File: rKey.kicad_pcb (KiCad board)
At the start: 2 copper layers, 52.8 x 66.8 mm, 42 parts, among them IC1 BDX34C, IC2 BDX34C, J1 Conn_01x03, Q1 BC337, Q2 BC337, Q3 BC337, Q4 BC337, Q5 BC327, Q8 BC337, U1 TL084BCN, U2 LM7810_TO220

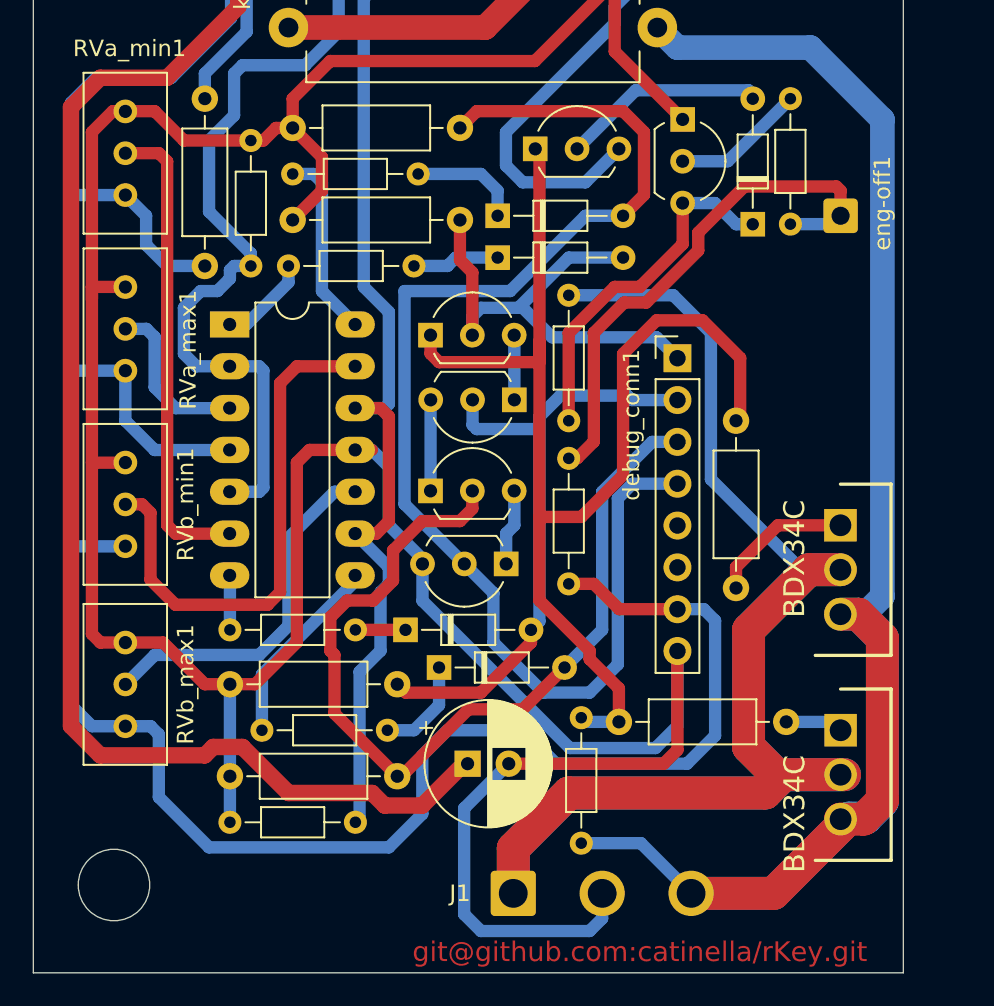
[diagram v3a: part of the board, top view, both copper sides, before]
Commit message: Fix: wrong resistors power size
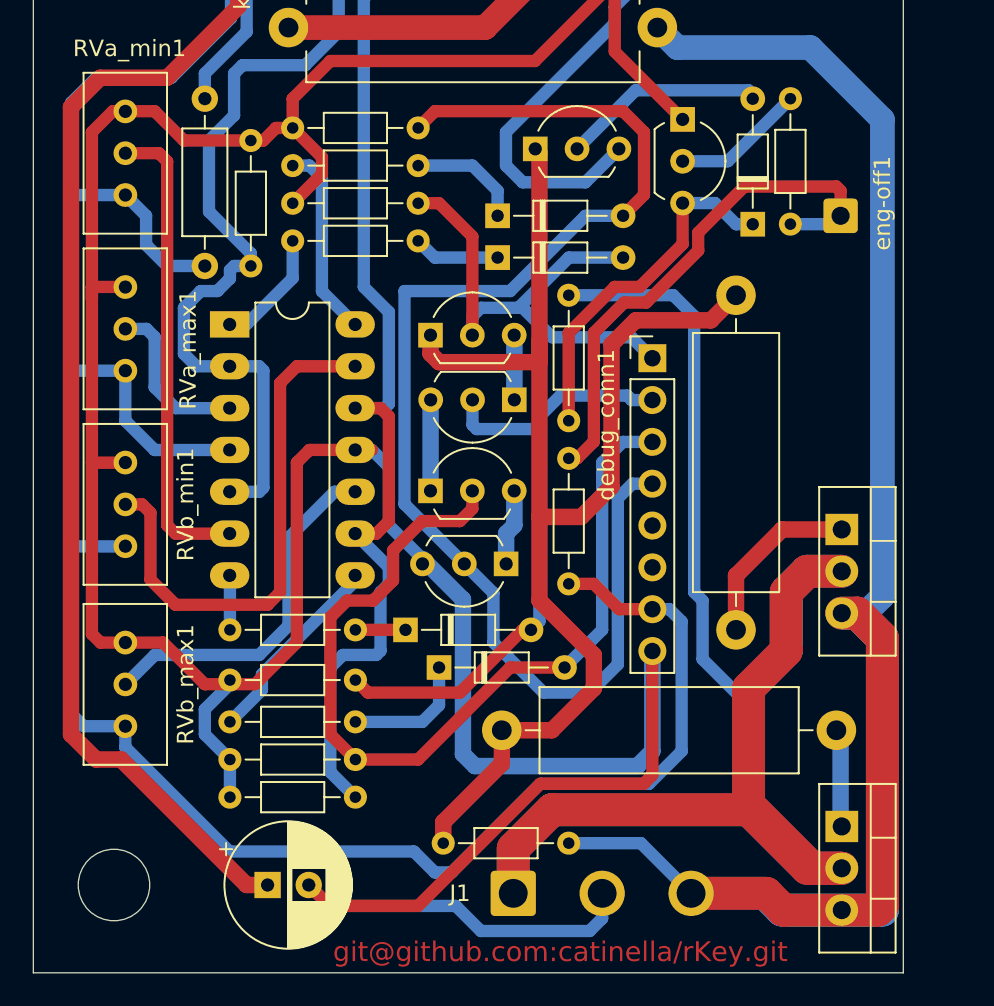
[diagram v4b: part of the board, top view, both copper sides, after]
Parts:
- removed IC1, IC2: BDX34C, BDX34C:TO270P460X1020X2008-3P
- added Q6: D45VH10, Package_TO_SOT_THT:TO-220-3_Vertical, F.Cu at (165.7, 96.5)
- added Q7: D45VH10, Package_TO_SOT_THT:TO-220-3_Vertical, F.Cu at (165.7, 114.6)
- R10, R18: value 1.6K -> 100; footprint Resistor_THT:R_Axial_DIN0207_L6.3mm_D2.5mm_P10.16mm_Horizontal -> Resistor_THT:R_Axial_DIN0516_L15.5mm_D5.0mm_P20.32mm_Horizontal
- R12, R15, R16, R17: footprint Resistor_THT:R_Axial_DIN0207_L6.3mm_D2.5mm_P10.16mm_Horizontal -> Resistor_THT:R_Axial_DIN0204_L3.6mm_D1.6mm_P7.62mm_Horizontal
- moved C1 14.2 mm to (130.8, 118.1)
- moved R18 7.62 mm to (159.3, 82.3)
- moved R10 7.13 mm to (145.0, 108.7)
- moved R4 2.01 mm to (128.5, 108.2)
- moved R2 1.55 mm to (132.3, 79.0)
- moved R8 1.52 mm to (136.1, 112.8)
- moved debug_conn1 1.52 mm to (154.2, 86.1)
- moved R15 1.02 mm to (132.3, 76.7)
- moved R16 1.02 mm to (128.5, 110.5)
- moved R11 0.76 mm to (149.1, 115.6), turned to 180 degrees
- moved R5 0.51 mm to (132.3, 74.4)
- moved R17 0.25 mm to (128.5, 105.7)
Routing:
- net GND: track 234.6 -> 253.1 mm
- net Net-(J1-Pad1): track 119.3 -> 132.7 mm
- net Net-(C1-Pad1): track 116.5 -> 105.2 mm
- net Net-(J1-Pad3): track 110.1 -> 119.7 mm
- net Net-(R1-Pad1): track 167.9 -> 160.7 mm
- net Net-(Q1-Pad1): track 74.7 -> 81.0 mm
- net Net-(R10-Pad2): track 3.51 -> 5.87 mm
- net Net-(R18-Pad2): track 8.66 -> 10.9 mm
- net Net-(R4-Pad2): track 6.05 -> 7.79 mm
- net Net-(R2-Pad1): track 5.63 -> 7.25 mm
- net Net-(Q1-Pad2): track 29.7 -> 31.0 mm
- net Net-(Q4-Pad2): track 80.1 -> 81.1 mm
- net Net-(R8-Pad1): track 62.7 -> 63.6 mm
- net Net-(Q2-Pad2): track 38.2 -> 38.9 mm

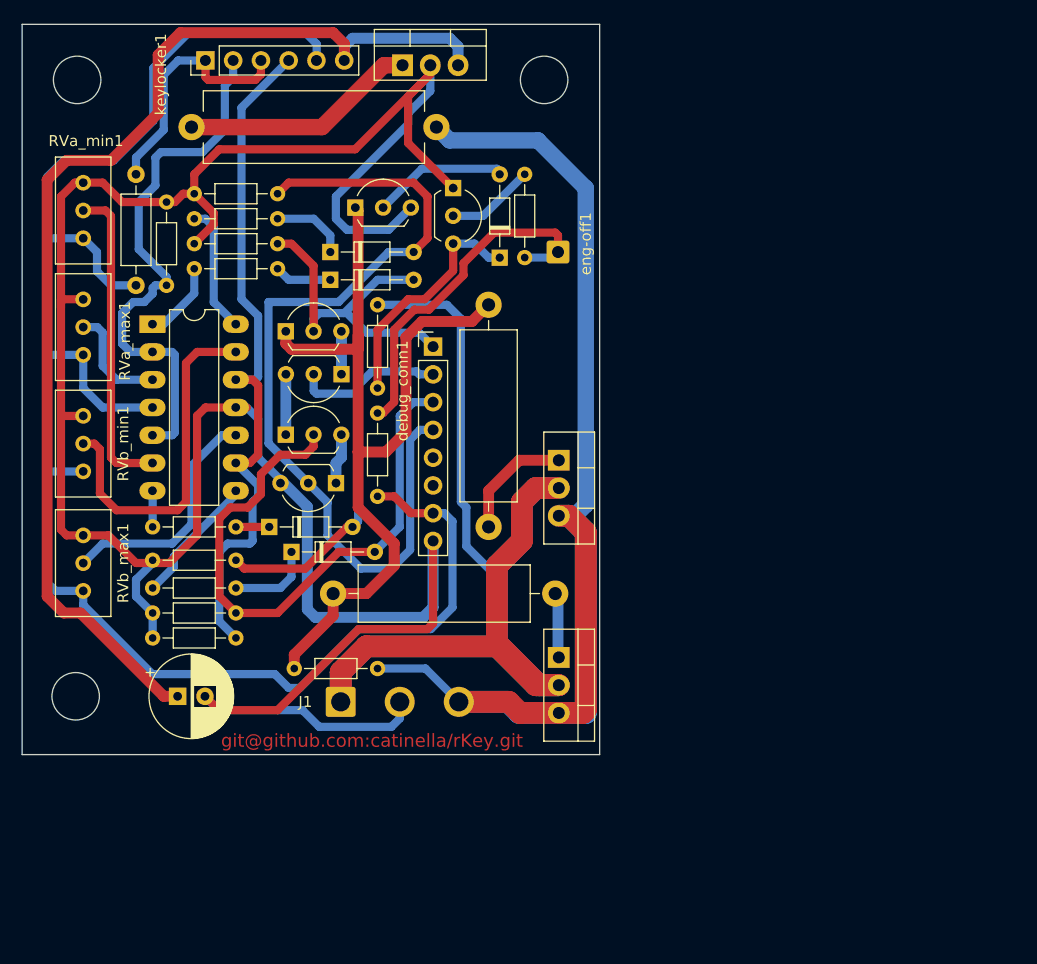
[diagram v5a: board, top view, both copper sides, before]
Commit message: Feat: Circuit for engine locking when vehicle is off
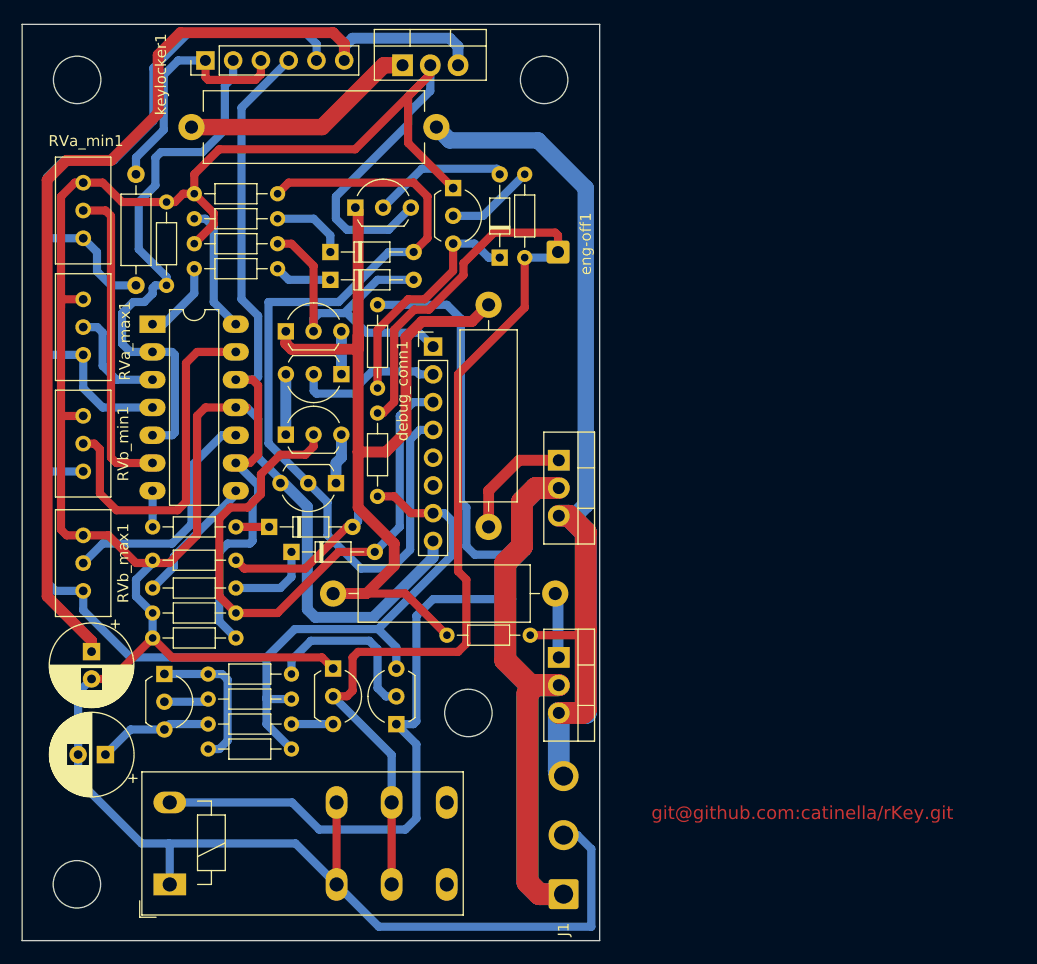
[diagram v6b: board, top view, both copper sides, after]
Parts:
- added C2: 2uF, Capacitor_THT:CP_Radial_D7.5mm_P2.50mm, F.Cu at (124.2, 123.4)
- added K1: RT42xxxx, Relay_THT:Relay_DPDT_Schrack-RT2-FormC_RM5mm, F.Cu at (130.1, 135.3)
- added Q10: BC337, Package_TO_SOT_THT:TO-92L_Inline_Wide, F.Cu at (129.6, 116.1)
- added Q11: BC327, Package_TO_SOT_THT:TO-92L_Inline_Wide, F.Cu at (145.0, 115.6)
- added Q9: BC327, Package_TO_SOT_THT:TO-92L_Inline_Wide, F.Cu at (150.8, 120.7)
- added R19: 60K, Resistor_THT:R_Axial_DIN0204_L3.6mm_D1.6mm_P7.62mm_Horizontal, F.Cu at (133.6, 118.4)
- added R20: 20K, Resistor_THT:R_Axial_DIN0204_L3.6mm_D1.6mm_P7.62mm_Horizontal, F.Cu at (133.6, 116.1)
- added R21: 2K, Resistor_THT:R_Axial_DIN0204_L3.6mm_D1.6mm_P7.62mm_Horizontal, F.Cu at (133.6, 120.7)
- added R22: 200K, Resistor_THT:R_Axial_DIN0204_L3.6mm_D1.6mm_P7.62mm_Horizontal, F.Cu at (141.2, 122.9)
- moved J1 26.9 mm to (166.1, 136.2), turned to 90 degrees
- moved R11 14.3 mm to (163.1, 112.5)
- moved C1 8.87 mm to (122.9, 114.0), turned to -90 degrees
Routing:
- net Net-(R13-Pad2): track 32.7 -> 106.3 mm
- net Net-(J1-Pad1): track 132.7 -> 186.5 mm
- net GND: track 253.1 -> 305.9 mm
- net Net-(J1-Pad3): track 119.7 -> 103.1 mm
- net Net-(Q9-Pad2): track 0.00 -> 15.8 mm
- net Net-(Q10-Pad1): track 0.00 -> 13.7 mm
- net Net-(R1-Pad1): track 160.7 -> 171.6 mm
- net Net-(C2-Pad1): track 0.00 -> 10.6 mm
- net Net-(C1-Pad1): track 105.2 -> 96.2 mm
- net Net-(Q10-Pad2): track 0.00 -> 4.11 mm
- net Net-(Q11-Pad3): track 0.00 -> 3.81 mm
- net Net-(Q1-Pad1): track 81.0 -> 84.7 mm
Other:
- board size 52.8 x 66.8 mm -> 52.8 x 83.8 mm

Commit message: fixes
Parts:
- added R23: 10K, Resistor_THT:R_Axial_DIN0204_L3.6mm_D1.6mm_P5.08mm_Horizontal, F.Cu at (148.3, 122.9)
- moved K1 0.25 mm to (130.1, 135.1)
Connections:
- K1 pad 11: Net-(R13-Pad2) -> Net-(K1-Pad11)
- K1 pad 21: Net-(R13-Pad2) -> Net-(K1-Pad11)
- Q11 pad 2: Net-(R13-Pad2) -> Net-(Q11-Pad2)
- R13 pad 2: Net-(R13-Pad2) -> Net-(K1-Pad11)
- R14 pad 2: Net-(R13-Pad2) -> Net-(K1-Pad11)
- eng-off1 pad 1: Net-(R13-Pad2) -> Net-(K1-Pad11)
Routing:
- net Net-(R13-Pad2): track 106.3 -> 0.00 mm
- net Net-(K1-Pad11): track 0.00 -> 100.9 mm
- net Net-(Q11-Pad2): track 0.00 -> 6.64 mm
- net Net-(Q9-Pad3): track 171.6 -> 173.7 mm

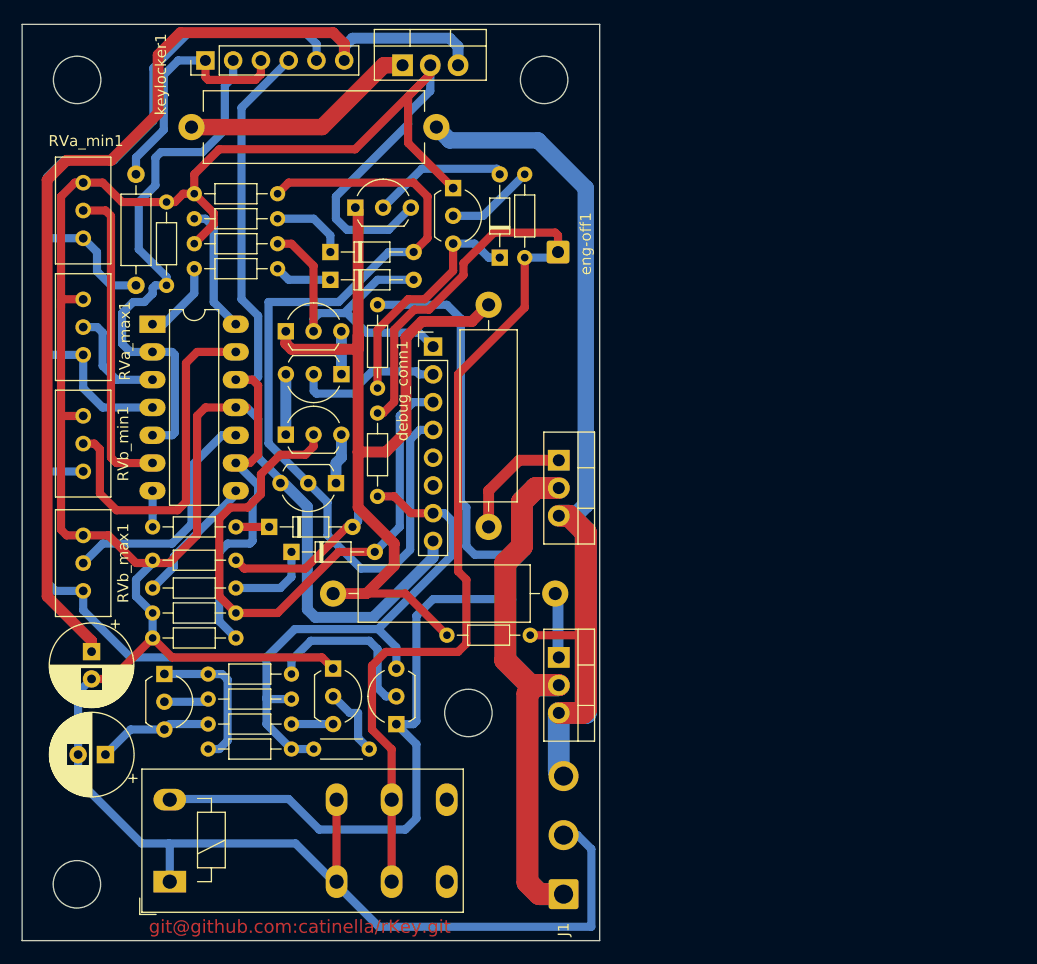
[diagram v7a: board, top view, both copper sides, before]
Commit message: PCB size reducing
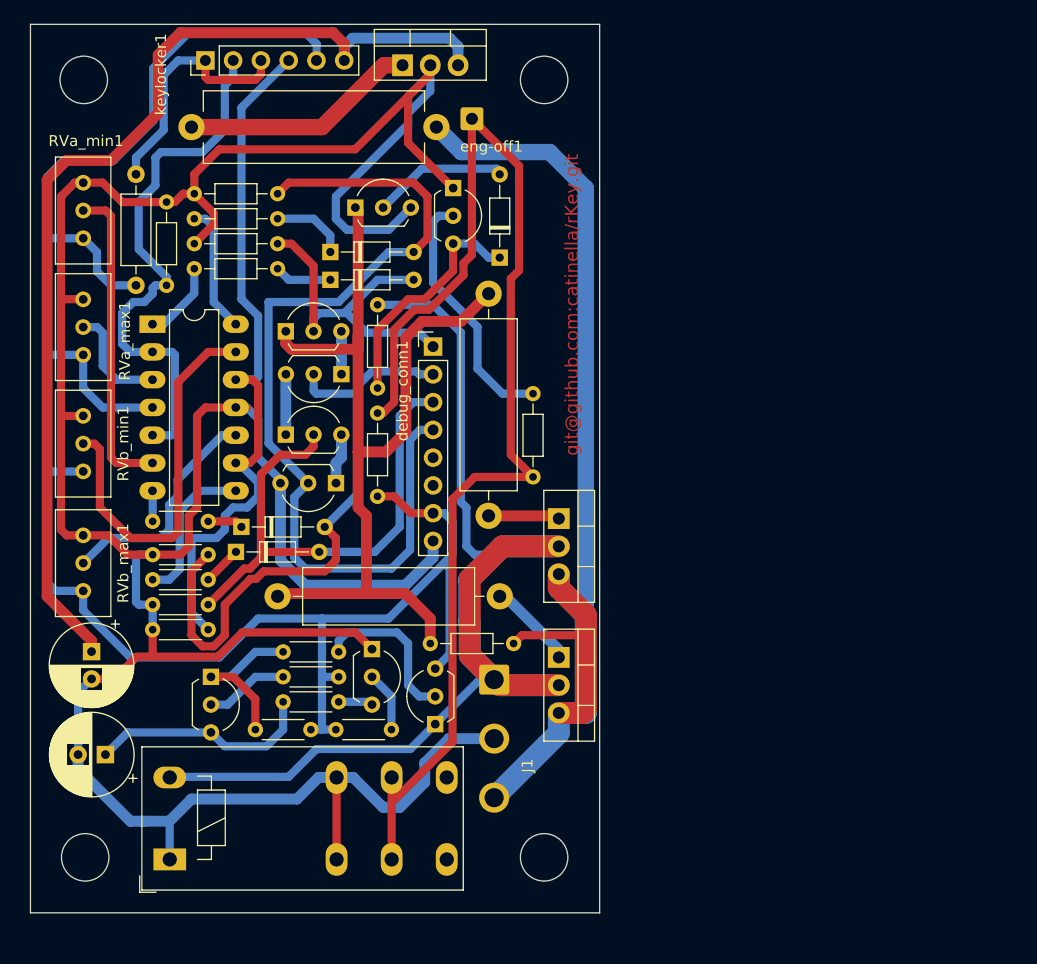
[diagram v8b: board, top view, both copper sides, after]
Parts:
- R16, R17, R19, R20, R21, R22, R3, R4, R8: footprint Resistor_THT:R_Axial_DIN0204_L3.6mm_D1.6mm_P7.62mm_Horizontal -> Resistor_THT:R_Axial_DIN0204_L3.6mm_D1.6mm_P5.08mm_Horizontal
- moved J1 20.6 mm to (159.8, 116.6), turned to -90 degrees
- moved R13 20.1 mm to (163.3, 90.4)
- moved eng-off1 14.5 mm to (157.7, 65.3)
- moved R19 7.15 mm to (140.5, 116.3)
- moved R21 7.15 mm to (140.5, 118.6)
- moved R20 7.15 mm to (140.5, 114.0)
- moved Q6 5.33 mm to (165.7, 101.9)
- moved R10 5.09 mm to (140.0, 109.0)
- moved ZD3 5.08 mm to (136.1, 104.9)
- moved Q10 4.27 mm to (133.9, 116.3)
- moved Q11 3.98 mm to (148.6, 113.8)
- moved Q9 3.56 mm to (154.4, 120.7)
- moved R23 2.70 mm to (150.4, 121.2)
- moved R8 2.65 mm to (133.6, 112.0)
- moved ZD2 2.54 mm to (136.6, 102.6)
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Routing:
- net Net-(J1-Pad1): track 186.3 -> 116.2 mm
- net Net-(Q2-Pad2): track 38.9 -> 57.4 mm
- net Net-(Q5-Pad2): track 8.12 -> 23.2 mm
- net GND: track 305.7 -> 291.9 mm
- net Net-(K1-Pad11): track 100.9 -> 112.1 mm
- net Net-(C2-Pad1): track 10.6 -> 20.8 mm
- net Net-(Q9-Pad3): track 173.7 -> 180.2 mm
- net Net-(Q3-Pad2): track 54.8 -> 48.6 mm
- net Net-(Q6-Pad1): track 10.9 -> 6.53 mm
- net Net-(R4-Pad2): track 7.79 -> 3.59 mm
- net Net-(Q4-Pad2): track 81.1 -> 85.1 mm
- net Net-(Q10-Pad2): track 4.11 -> 7.66 mm
- net Net-(RVb_min1-Pad2): track 32.3 -> 35.7 mm
- net Net-(Q7-Pad1): track 5.87 -> 8.12 mm
- net Net-(R4-Pad1): track 12.0 -> 14.1 mm
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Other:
- board size 52.8 x 83.8 mm -> 52.1 x 81.3 mm
